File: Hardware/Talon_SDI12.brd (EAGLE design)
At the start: 140 x 19 mm, 123 parts, among them J1 CONN_APOGEE_LOGGER, J2 CONN_TALON_REMOTE, J3 CONN_SDI-12_LOGGERM8_TE_BOARD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, J4 CONN_SDI-12_LOGGERM8_TE_BOARD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, J5 CONN_SDI-12_LOGGERM8_TE_BOARD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, Q1 2N7002, Q2 2N7002, Q3 2N7002, Q4 2N7002, Q5 AO3419, Q6 AO3419, Q7 AO3419, Q8 AO3419, U1 SN74HC04, U10 FXMAR2102UMLP, U11 74HC4852, U12 SN74LVC1G3157SC70, U13 MCP3221, U14 MCP23018QFN, U15 PCA9536DFN, U16 MCP3421A3, U17 SN74LVC1G3157SC70, U18 SN74LVC1G3157SC70, U19 SN74LVC1G3157SC70, U2 CD4044, U20 SN74LVC1G3157SC70, U21 SN74LVC1G00SC70, U22 SN74LVC2G241DCU, U23 SN74LVC1G17DCK, U24 24AA02SOT23, U3 SIP32431TDFN, U4 INA4180A2, U5 MAX9034TSSOP, U6 SI1869, U7 SN74AC08, U8 LM2621, U9 LMR62014SOT23

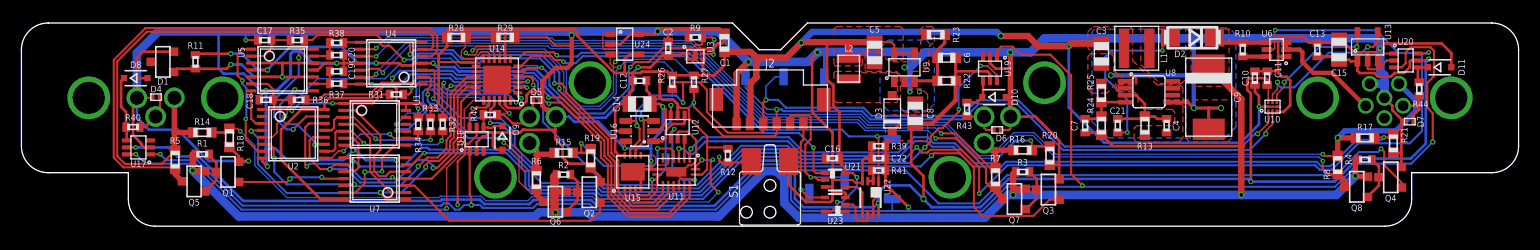
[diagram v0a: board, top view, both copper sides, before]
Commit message: v1.1 Updates
moved port 1 and port 4, sent to fab
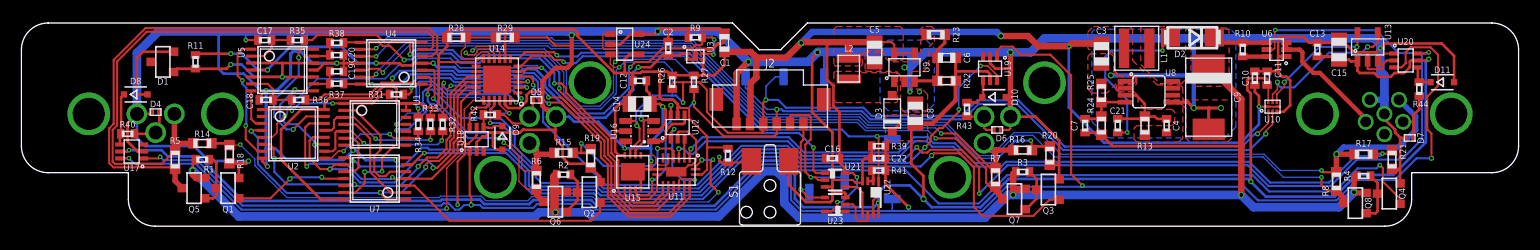
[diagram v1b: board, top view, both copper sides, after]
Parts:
- moved R17 1.53 mm to (55.5, 6.73)
- moved Q4 1.53 mm to (57.9, 3.05)
- moved R21 1.53 mm to (58.2, 6.22)
- moved R4 1.53 mm to (55.5, 4.70)
- moved Q8 1.53 mm to (54.7, 2.16)
- moved R8 1.53 mm to (53.0, 4.19)
- moved R18 1.52 mm to (-50.5, 6.73)
- moved Q1 1.52 mm to (-50.7, 3.56)
- moved D7 1.52 mm to (59.8, 8.26)
- moved D8 1.52 mm to (-59.3, 12.3)
- moved J1 1.50 mm to (57.5, 10.5)
- moved J3 1.50 mm to (-57.5, 10.5)
- moved D11 1.42 mm to (62.9, 13.5)
- moved D4 1.40 mm to (-57.5, 10.7)
- moved R14 1.02 mm to (-53.1, 7.75)
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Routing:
- net GND: track 446.9 -> 450.8 mm
- net DATA: track 177.5 -> 180.2 mm
- net !DATA_EN4: track 140.1 -> 141.8 mm
- net 5V: track 199.4 -> 201.1 mm
- net SENSE1+: track 51.6 -> 53.1 mm
- net VPORT1_OUT_SENSE: track 57.9 -> 56.5 mm
- net DATA_OUT_PROTEC1: track 6.16 -> 4.84 mm
- net DATA_OUT4: track 4.16 -> 5.14 mm
- net VPORT4_OUT: track 113.2 -> 114.0 mm
- net VHEATER: track 10.8 -> 11.6 mm
- net N$2: track 4.21 -> 5.00 mm
- net MOS_CTRL1: track 10.0 -> 10.7 mm
- net VPORT1_OUT: track 55.0 -> 54.4 mm
- net N$4: track 4.21 -> 4.73 mm
- net SENSE4+: track 100.9 -> 101.4 mm
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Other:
- board text added: "Talon - SDI-12 v1.1 Bobby Schulz"
- board text removed: "Talon - SDI-12 v1.0 Bobby Schulz"

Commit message: v1.2 updates
Fixed physical overlap in current limit circuit
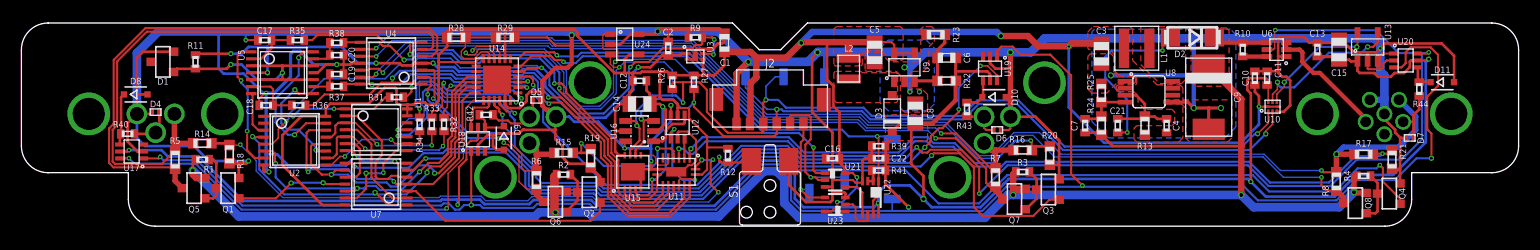
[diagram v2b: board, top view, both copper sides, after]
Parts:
- moved U2 0.65 mm to (-44.5, 8.00)
- moved U1 0.52 mm to (-36.8, 9.02)
- moved U7 0.52 mm to (-36.8, 3.94)
- moved C18 0.51 mm to (-47.1, 11.3)
- moved R36 0.51 mm to (-44.1, 11.3)
- moved R42 0.38 mm to (-26.5, 10.4)
- moved R31 0.25 mm to (-34.9, 12.1)
- moved R37 0.25 mm to (-40.5, 13.1)
- moved C19 0.25 mm to (-40.5, 14.2)
- moved U5 0.25 mm to (-45.6, 14.4)
- moved R34 0.13 mm to (-32.8, 9.53)
- moved D9 0.13 mm to (-24.9, 8.26)
- moved R32 0.13 mm to (-30.5, 9.53)
- moved R33 0.13 mm to (-31.6, 9.53)
- moved U18 0.13 mm to (-27.3, 8.13)
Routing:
- net DATA_EN4: track 17.5 -> 19.0 mm
- net !DATA_EN4: track 141.8 -> 143.2 mm
- net 3V3_SENSE: track 56.1 -> 57.2 mm
- net EN2: track 35.9 -> 37.0 mm
- net LATCH1: track 11.8 -> 12.6 mm
- net DATA_EN3: track 62.4 -> 61.6 mm
- net 3V3: track 212.3 -> 213.0 mm
- net EN1: track 31.1 -> 31.7 mm
- net FAULT3: track 14.4 -> 14.9 mm
- net FAULT1: track 10.4 -> 11.0 mm
- net FAULT2: track 12.5 -> 13.1 mm
- net LATCH3: track 10.4 -> 10.9 mm
- net GND: track 450.8 -> 451.4 mm
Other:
- board text added: "Talon - SDI-12 v1.2 Bobby Schulz"
- board text removed: "Talon - SDI-12 v1.1 Bobby Schulz"

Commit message: v1.3 Updates
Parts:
- R18, R19, R20, R21: device bschulz_passives:R0603 -> bschulz_passives:R0402
- moved Q2 0.89 mm to (-16.9, 2.29)
- moved Q3 0.89 mm to (26.0, 2.54)
- moved R18 0.64 mm to (-51.1, 7.11)
- moved R19 0.52 mm to (-17.3, 6.22)
- moved R20 0.52 mm to (25.7, 6.48)
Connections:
- net !DATA_EN4: no longer U6.5
- net DATA_EN4: now also U6.5
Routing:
- net DATA_EN4: track 19.0 -> 117.2 mm, vias 2 -> 5
- net !DATA_EN4: track 143.2 -> 125.9 mm, vias 5 -> 4
- net GND: track 451.4 -> 454.1 mm
- net MOS_CTRL2: track 20.4 -> 19.5 mm
- net POS_DETECT: track 30.2 -> 31.0 mm
- net !RX: track 3.91 -> 4.28 mm, vias 0 -> 2
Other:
- board text added: "Talon - SDI-12 v1.3 Bobby Schulz"
- board text removed: "Talon - SDI-12 v1.2 Bobby Schulz"

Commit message: Updates for BoM
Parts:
- C17, C18, C19, C20, C4: value 0.1uF -> DNP
- C21: value (none) -> 1pF
- C9: value 68uF -> 100uF
- D10, D11, D8, D9: value (none) -> 5.1V
- D4, D5, D6, D7: value 6V -> 12V
- R13: value 470k -> 390k

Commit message: Updated EEPROM part number
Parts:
- D10, D11, D8, D9: value 5.1V -> (none)
- U24: value 24AA02SOT23 -> AT24MAC602SOT23
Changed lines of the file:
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@@
 <attribute name="NAME" x="60.833" y="8.255" size="0.6096" layer="25" font="vector" ratio="15" rot="R90" align="center"/>
 </element>
-<element name="U24" library="bschulz" package="SOT23-5" value="24AA02SOT23" x="-13.589" y="17.018" smashed="yes" rot="R270">
-<attribute name="DIGIKEY" value="24AA025E64T-I/OTCT-ND" x="-12.319" y="17.018" size="1.27" layer="27" font="vector" ratio="15" rot="R270" display="off"/>
-<attribute name="DISP" value="24AA025E64" x="-12.319" y="17.018" size="1.27" layer="27" font="vector" ratio="15" rot="R270" display="off"/>
+<element name="U24" library="bschulz" package="SOT23-5" value="AT24MAC602SOT23" x="-13.589" y="17.018" smashed="yes" rot="R270">
+<attribute name="DIGIKEY" value="AT24MAC602-STUM-TCT-ND" x="-12.319" y="17.018" size="1.27" layer="27" font="vector" ratio="15" rot="R270" display="off"/>
+<attribute name="DISP" value="AT24MAC602" x="-12.319" y="17.018" size="1.27" layer="27" font="vector" ratio="15" rot="R270" display="off"/>
 <attribute name="MF" value="Microchip" x="-12.319" y="17.018" size="1.27" layer="27" font="vector" ratio="15" rot="R270" display="off"/>
-<attribute name="MOUSER" value="24AA025E64T-I/OTCT-ND" x="-12.319" y="17.018" size="1.27" layer="27" font="vector" ratio="15" rot="R270" display="off"/>
-<attribute name="MPN" value="24AA025E64T-I/OT" x="-12.319" y="17.018" size="1.27" layer="27" font="vector" ratio="15" rot="R270" display="off"/>
+<attribute name="MPN" value="AT24MAC602-STUM-T" x="-12.319" y="17.018" size="1.27" layer="27" font="vector" ratio="15" rot="R270" display="off"/>
 <attribute name="NAME" x="-11.938" y="17.018" size="0.6096" layer="25" font="vector" ratio="15" rot="R180" align="center"/>
 <attribute name="VALUE" x="-13.462" y="14.732" size="0.6096" layer="27" font="vector" ratio="15" align="center"/>
@@
 <attribute name="VALUE_PART" value="510" x="10.16" y="5.207" size="1.778" layer="27" rot="R180" display="off"/>
 </element>
-<element name="D8" library="bschulz" package="SOD323-R" value="5.1V" x="-59.309" y="12.319" smashed="yes">
+<element name="D8" library="bschulz" package="SOD323-R" value="" x="-59.309" y="12.319" smashed="yes">
 <attribute name="DIGIKEY" value="BZX384B5V1-HE3-08GICT-ND" x="-59.309" y="12.319" size="1.778" layer="27" display="off"/>
 <attribute name="MF" value="Vishay" x="-59.309" y="12.319" size="1.778" layer="27" display="off"/>
@@
 <attribute name="VALUE_PART" value="510" x="-26.543" y="10.414" size="1.778" layer="27" rot="R180" display="off"/>
 </element>
-<element name="D9" library="bschulz" package="SOD323-R" value="5.1V" x="-24.892" y="8.255" smashed="yes" rot="R270">
+<element name="D9" library="bschulz" package="SOD323-R" value="" x="-24.892" y="8.255" smashed="yes" rot="R270">
 <attribute name="DIGIKEY" value="BZX384B5V1-HE3-08GICT-ND" x="-24.892" y="8.255" size="1.778" layer="27" rot="R270" display="off"/>
 <attribute name="MF" value="Vishay" x="-24.892" y="8.255" size="1.778" layer="27" rot="R270" display="off"/>
@@
 <attribute name="VALUE_PART" value="510" x="18.415" y="10.922" size="1.778" layer="27" rot="R90" display="off"/>
 </element>
-<element name="D10" library="bschulz" package="SOD323-R" value="5.1V" x="20.955" y="12.065" smashed="yes">
+<element name="D10" library="bschulz" package="SOD323-R" value="" x="20.955" y="12.065" smashed="yes">
 <attribute name="DIGIKEY" value="BZX384B5V1-HE3-08GICT-ND" x="20.955" y="12.065" size="1.778" layer="27" display="off"/>
 <attribute name="MF" value="Vishay" x="20.955" y="12.065" size="1.778" layer="27" display="off"/>
@@
 <attribute name="VALUE_PART" value="510" x="60.706" y="12.827" size="1.778" layer="27" rot="R90" display="off"/>
 </element>
-<element name="D11" library="bschulz" package="SOD323-R" value="5.1V" x="62.865" y="13.462" smashed="yes">
+<element name="D11" library="bschulz" package="SOD323-R" value="" x="62.865" y="13.462" smashed="yes">
 <attribute name="DIGIKEY" value="BZX384B5V1-HE3-08GICT-ND" x="62.865" y="13.462" size="1.778" layer="27" display="off"/>
 <attribute name="MF" value="Vishay" x="62.865" y="13.462" size="1.778" layer="27" display="off"/>

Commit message: Updated to v1.4
Added loopback functionality, replaced MCP23018 with PACL9535A, fixed inverter (U23) model, fixed attributes on schematics
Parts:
- removed R28: 110k, bschulz_passives:R0603
- removed R29: 49.9k, bschulz_passives:R0603
- added U25: SN74AUP1T87, bschulz:DCK_R-PDSO-G5
- U14: value MCP23018QFN -> PCAL9535AQFN
- U23: value SN74LVC1G17DCK -> (none)
- moved R42 0.18 mm to (-26.4, 10.3)
- moved U14 0.13 mm to (-25.5, 13.8), turned to 0 degrees
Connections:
- removed net N$14: R28.1, R29.2, U14.11
- new net DIR_BYPASS: U22.7, U25.4
- net 3V3: now also U14.18, U14.21, U14.24, U25.5; no longer R28.2, U14.12, U14.8
- net DATA_EN1: now also U14.5; no longer U14.19
- net DATA_EN2: now also U14.6; no longer U14.20
- net DATA_EN3: now also U14.7; no longer U14.21
- net DATA_EN4: now also U14.8; no longer U14.22
- net DIR: now also U14.17, U25.1; no longer U14.7, U22.7
- net EN1: now also U14.1; no longer U14.15
- net EN2: now also U14.2; no longer U14.16
- net EN3: now also U14.3; no longer U14.17
- net EN4: now also U14.4; no longer U14.18
- net FAULT1_SENSE: now also U14.10; no longer U14.24
- net FAULT2_SENSE: now also U14.11; no longer U14.1
- net FAULT3_SENSE: now also U14.12; no longer U14.2
- net FAULT4_SENSE: now also U14.13; no longer U14.3
- net FOUT: now also U14.16; no longer U14.6
- net GND: now also U14.9, U25.3; no longer R29.1
- net MUX_EN: now also U25.2
- net POS_DETECT: now also U14.14; no longer U14.4
- net SCL: now also U14.19; no longer U14.9
- net SDA: now also U14.20; no longer U14.10
- net SENSE_EN: now also U14.15; no longer U14.5
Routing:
- net MUX_EN: track 3.78 -> 30.4 mm, vias 0 -> 4
- net N$14: track 8.24 -> 0.00 mm
- net 3V3: track 212.7 -> 219.1 mm, vias 6 -> 7
- net N$38: track 9.53 -> 12.7 mm
- net DIR_BYPASS: track 0.00 -> 2.97 mm
- net DATA_EN3: track 61.6 -> 64.3 mm
- net VPORT1_OUT_SENSE: track 57.0 -> 59.6 mm
- net SCL: track 119.5 -> 121.6 mm
- net SDA: track 118.1 -> 119.8 mm
- net POS_DETECT: track 31.0 -> 29.8 mm
- net DATA: track 180.1 -> 181.3 mm
- net EN4: track 28.5 -> 29.6 mm
- net EN1: track 31.7 -> 32.7 mm
- net EN2: track 37.0 -> 38.0 mm
- net GND: track 454.1 -> 455.0 mm
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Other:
- board text added: "Talon - SDI-12 v1.4 Bobby Schulz"
- board text removed: "Talon - SDI-12 v1.3 Bobby Schulz"
